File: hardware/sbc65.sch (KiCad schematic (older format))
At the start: 22 parts

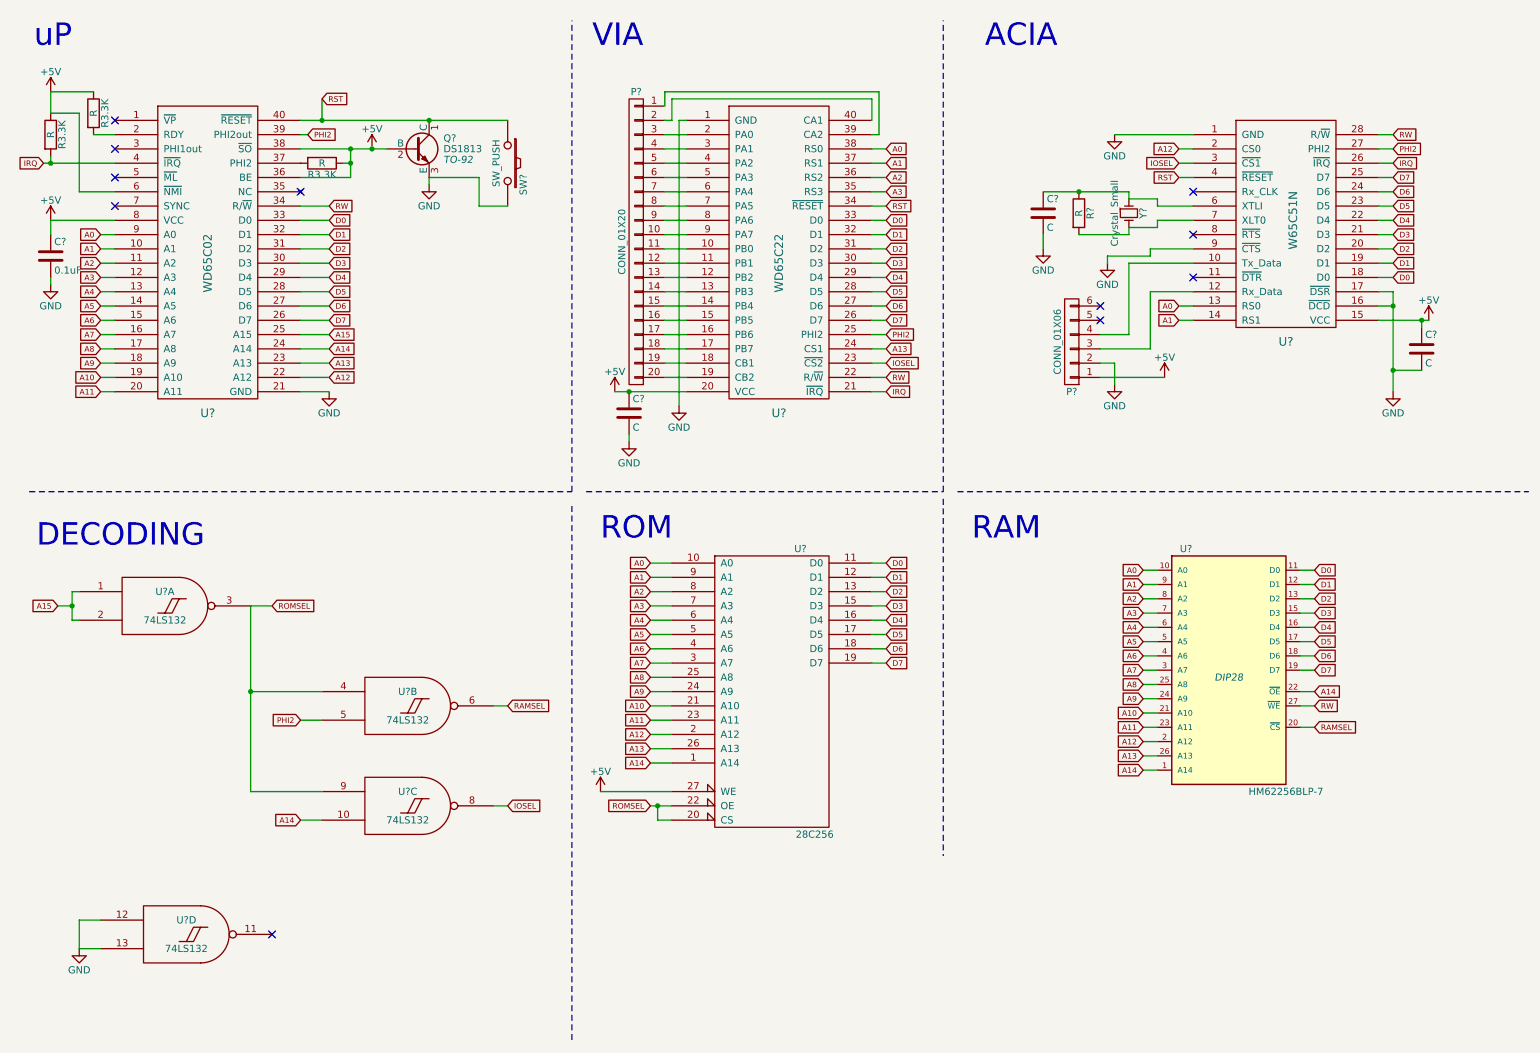
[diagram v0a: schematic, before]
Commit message: Trying to fix ACIA Xmit issues, added more to schematics
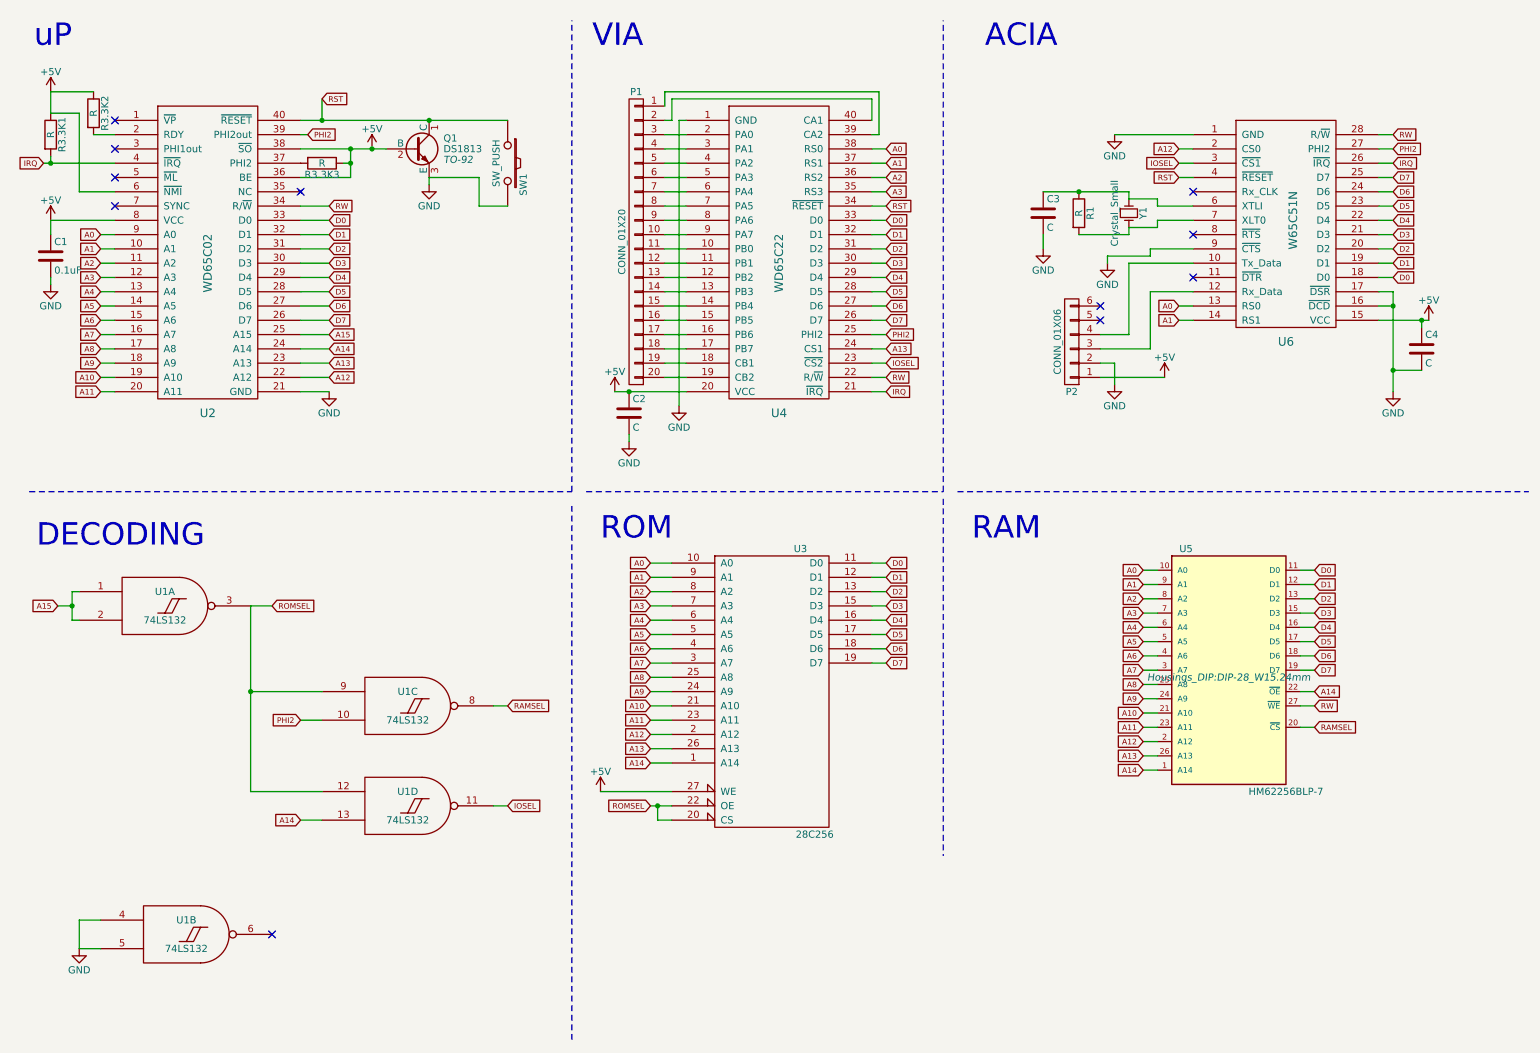
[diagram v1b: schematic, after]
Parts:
- C1, C2, C3, C4: renamed from C?; footprint (none) -> Capacitors_ThroughHole:C_Disc_D3_P2.5
- P1: renamed from P?; footprint (none) -> Pin_Headers:Pin_Header_Straight_1x20
- P2: renamed from P?; footprint (none) -> Pin_Headers:Pin_Header_Straight_1x06
- R1: renamed from R?; footprint (none) -> Resistors_ThroughHole:Resistor_Horizontal_RM7mm
- R3.3K1, R3.3K2, R3.3K3: renamed from R3.3K; footprint (none) -> Resistors_ThroughHole:Resistor_Horizontal_RM7mm
- SW1: renamed from SW?; footprint (none) -> Buttons_Switches_ThroughHole:SW_PUSH
- U1: renamed from U?; footprint (none) -> Housings_DIP:DIP-14_W7.62mm
- U2, U4: renamed from U?; footprint (none) -> Housings_DIP:DIP-40_W25.4mm
- U3, U6: renamed from U?; footprint (none) -> Housings_DIP:DIP-28_W15.24mm
- U5: renamed from U?; footprint DIP28 -> Housings_DIP:DIP-28_W15.24mm
- Y1: renamed from Y?; footprint (none) -> Crystals:Crystal_HC49-U_Vertical
- gave numbers to parts that had none: 1
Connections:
- net A14: now also U1.13; no longer U1.10
- net GND: now also U1.4, U1.5; no longer U1.12, U1.13
- net IOSEL: now also U1.11; no longer U1.8
- net PHI2: now also U1.10; no longer U1.5
- net RAMSEL: now also U1.8; no longer U1.6
- net ROMSEL: now also U1.12, U1.9; no longer U1.4, U1.9
